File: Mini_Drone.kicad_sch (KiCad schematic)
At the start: 78 parts, among them J1 Conn_01x02, J3 Conn_01x02, J4 Conn_01x06, J7 Conn_01x11, J8 Conn_01x11, Q1 AO3400A, Q2 AO3400A, Q3 AO3400A, Q4 AO3400A, U1 ESP32-S3-WROOM-1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

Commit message: final checking and then order
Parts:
- removed R10, R12, R13, R14: 220, Resistor_SMD:R_0201_0603Metric, symbol Mini_Drone_prj:R
- added R12, R15, R16, R17: 220, Resistor_SMD:R_0603_1608Metric, symbol Device:R
- S2: footprint 500SSP1S1M2REA:SW_500SSP1S1M2REA -> Mini_Drone_prj:slide swithc
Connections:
- net BAT+: now also R12.1
- net GND: now also R15.1, R16.1, R17.1
- net at D5.1 (K): now also R17.2
- net at D1.1 (K): now also R16.2
- net at D7.1 (K): now also R15.2
- net at D8.2 (A): now also R12.2

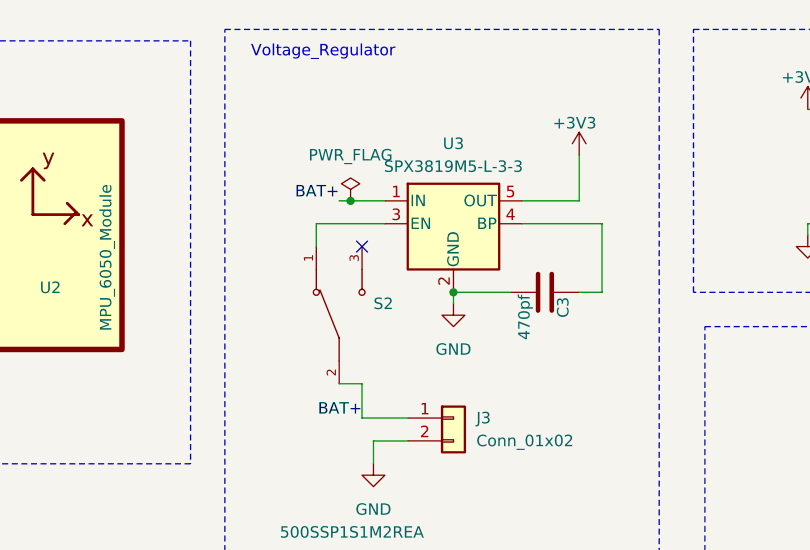
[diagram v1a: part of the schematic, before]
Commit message: added gnd to the switch other terminal
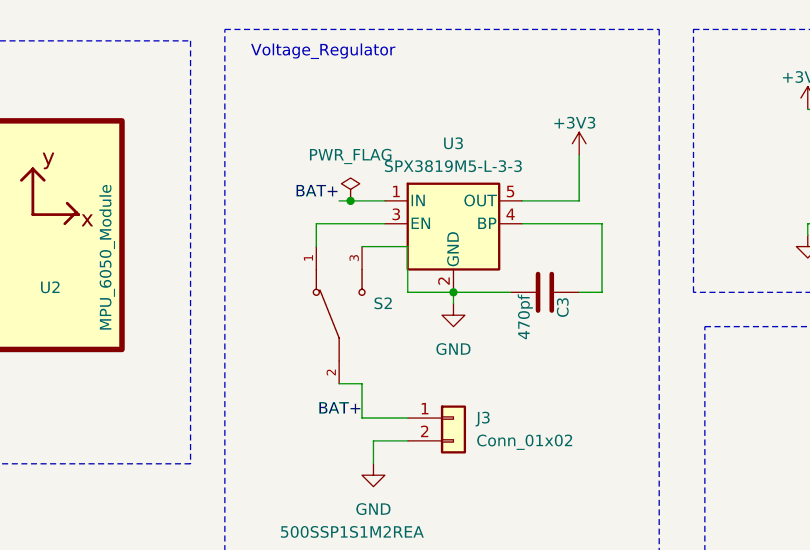
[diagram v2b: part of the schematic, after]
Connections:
- net GND: now also S2.3
- no-connect marks 5 -> 4
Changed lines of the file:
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@@
-	)
-	(no_connect
-		(at 207.01 43.18)
 	)
 	(no_connect
@@
 	(wire
 		(pts
+			(xy 212.09 48.26) (xy 217.17 48.26)
+		)
+		(stroke
+			(width 0)
+			(type default)
+		)
+	)
+	(wire
+		(pts
 			(xy 30.48 242.57) (xy 39.37 242.57)
 		)
@@
 	(wire
 		(pts
+			(xy 207.01 43.18) (xy 212.09 43.18)
+		)
+		(stroke
+			(width 0)
+			(type default)
+		)
+	)
+	(wire
+		(pts
 			(xy 243.84 236.22) (xy 243.84 232.41)
 		)
@@
 		)
 		(stroke
+			(width 0)
+			(type default)
+		)
+	)
+	(wire
+		(pts
+			(xy 212.09 43.18) (xy 212.09 48.26)
+		)
+		(stroke

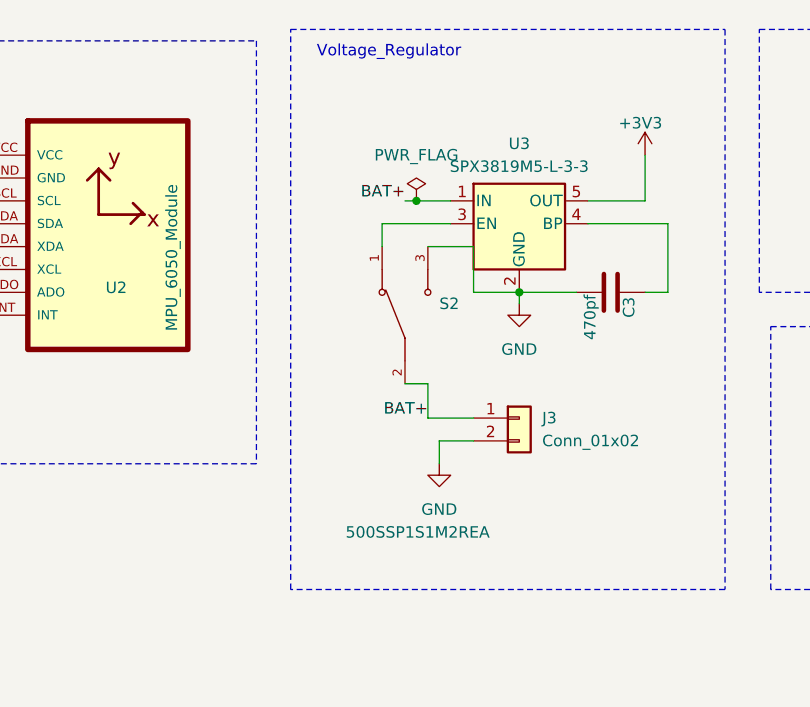
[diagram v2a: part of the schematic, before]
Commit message: switch connection has been corrected and the  polygon pour  has been reduced  to one layer for gnd and the connection is set to thermaal relief  for  easier soldering
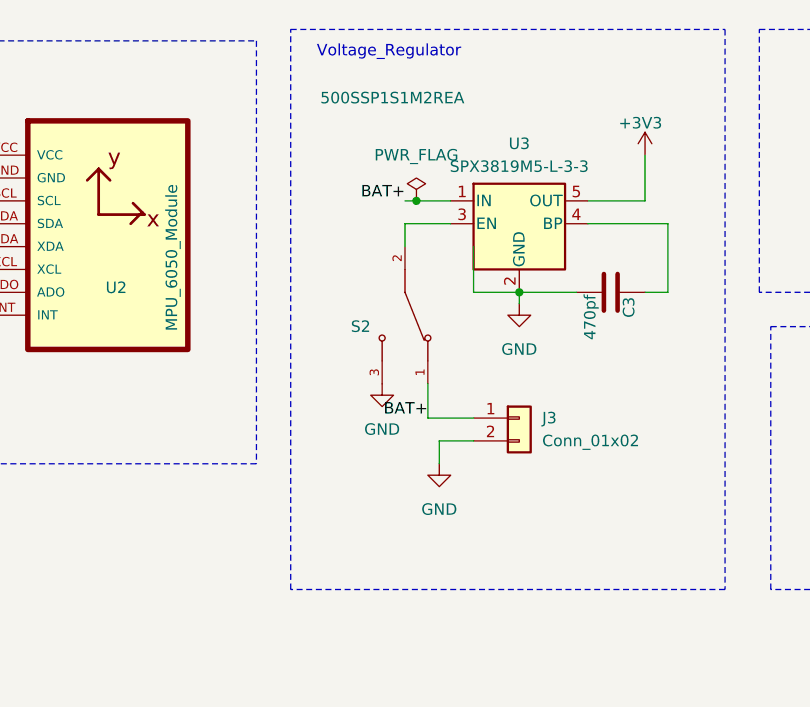
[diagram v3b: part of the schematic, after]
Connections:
- net BAT+: now also S2.1; no longer S2.2
- net at U3.3 (EN): now also S2.2; no longer S2.1
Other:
- moved on the sheet: S2
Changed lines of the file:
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@@
 	(wire
 		(pts
-			(xy 201.93 43.18) (xy 201.93 40.64)
-		)
-		(stroke
-			(width 0)
-			(type default)
-		)
-	)
-	(wire
-		(pts
 			(xy 39.37 242.57) (xy 48.26 242.57)
 		)
@@
 	(wire
 		(pts
-			(xy 207.01 43.18) (xy 212.09 43.18)
-		)
-		(stroke
-			(width 0)
-			(type default)
-		)
-	)
-	(wire
-		(pts
 			(xy 243.84 236.22) (xy 243.84 232.41)
 		)
@@
 	(wire
 		(pts
-			(xy 207.01 58.42) (xy 207.01 62.23)
+			(xy 160.02 227.33) (xy 166.37 227.33)
 		)
 		(stroke
@@
 	(wire
 		(pts
-			(xy 160.02 227.33) (xy 166.37 227.33)
+			(xy 31.75 90.17) (xy 31.75 87.63)
 		)
 		(stroke
@@
 	(wire
 		(pts
-			(xy 31.75 90.17) (xy 31.75 87.63)
+			(xy 148.59 132.08) (xy 148.59 137.16)
 		)
 		(stroke
@@
 	(wire
 		(pts
-			(xy 148.59 132.08) (xy 148.59 137.16)
+			(xy 204.47 43.18) (xy 204.47 40.64)
+		)
+		(stroke
+			(width 0)
+			(type default)
+		)
+	)
+	(wire
+		(pts
+			(xy 204.47 40.64) (xy 209.55 40.64)
 		)
 		(stroke
@@
 	(wire
 		(pts
-			(xy 31.75 33.02) (xy 41.91 33.02)
+			(xy 207.01 58.42) (xy 207.01 62.23)
 		)
 		(stroke
@@
 	(wire
 		(pts
-			(xy 34.29 54.61) (xy 29.21 54.61)
+			(xy 31.75 33.02) (xy 41.91 33.02)
 		)
 		(stroke
@@
 	(wire
 		(pts
-			(xy 233.68 40.64) (xy 233.68 48.26)
+			(xy 34.29 54.61) (xy 29.21 54.61)
 		)
 		(stroke
@@
 	(wire
 		(pts
-			(xy 95.25 162.56) (xy 107.95 162.56)
+			(xy 233.68 40.64) (xy 233.68 48.26)
 		)
 		(stroke
@@
 	(wire
 		(pts
-			(xy 247.65 232.41) (xy 254 232.41)
+			(xy 95.25 162.56) (xy 107.95 162.56)
 		)
 		(stroke
@@
 	(wire
 		(pts
-			(xy 49.53 90.17) (xy 52.07 90.17)
+			(xy 247.65 232.41) (xy 254 232.41)
 		)
 		(stroke
@@
 	(wire
 		(pts
-			(xy 204.47 58.42) (xy 207.01 58.42)
+			(xy 49.53 90.17) (xy 52.07 90.17)
 		)
 		(stroke
@@
 	(wire
 		(pts
-			(xy 201.93 40.64) (xy 209.55 40.64)
-		)
-		(stroke
-			(width 0)
-			(type default)
-		)
-	)
-	(wire
-		(pts
 			(xy 224.79 228.6) (xy 224.79 224.79)
 		)
@@
 	)
 	(symbol
+		(lib_id "power:GND")
+		(at 201.93 58.42 0)
+		(unit 1)
+		(exclude_from_sim no)
+		(in_bom yes)
+		(on_board yes)
+		(dnp no)
+		(fields_autoplaced yes)
+		(property "Reference" "#PWR024"
+			(at 201.93 64.77 0)
+			(effects
+				(font
+					(size 1.27 1.27)
+				)
+				(hide yes)
+			)
+		)
+		(property "Value" "GND"
+			(at 201.93 63.5 0)
+			(effects
+				(font
+					(size 1.27 1.27)
+				)
+			)
+		)
+		(property "Footprint" ""
+			(at 201.93 58.42 0)
+			(effects
+				(font
+					(size 1.27 1.27)
+				)
+				(hide yes)
+			)
+		)
+		(property "Datasheet" ""
+			(at 201.93 58.42 0)
+			(effects
+				(font
+					(size 1.27 1.27)
+				)
+				(hide yes)
+			)
+		)
+		(property "Description" "Power symbol creates a global label with name \"GND\" , ground"
+			(at 201.93 58.42 0)
+			(effects
+				(font
+					(size 1.27 1.27)
+				)
+				(hide yes)
+			)
+		)
+		(pin "1"
+		)
+		(instances
+			(project "Mini_Drone"
+				(path "/d47445ad-10e9-49aa-a867-c91f8f8ff1e7"
+					(reference "#PWR024")
+					(unit 1)
+				)
+			)
+		)
+	)
+	(symbol
 		(lib_id "Connector:TestPoint")
 		(at 48.26 138.43 180)
@@
 	(symbol
 		(lib_id "Mini_Drone_prj:500SSP1S1M2REA")
-		(at 204.47 50.8 90)
+		(at 204.47 50.8 270)
 		(unit 1)
 		(exclude_from_sim no)
@@
 		(dnp no)
 		(property "Reference" "S2"
-			(at 208.28 49.5299 90)
+			(at 200.66 52.0701 90)
 			(effects
 				(font
@@
 		)
 		(property "Value" "500SSP1S1M2REA"
-			(at 197.866 74.93 90)
+			(at 211.074 26.67 90)
 			(effects
 				(font

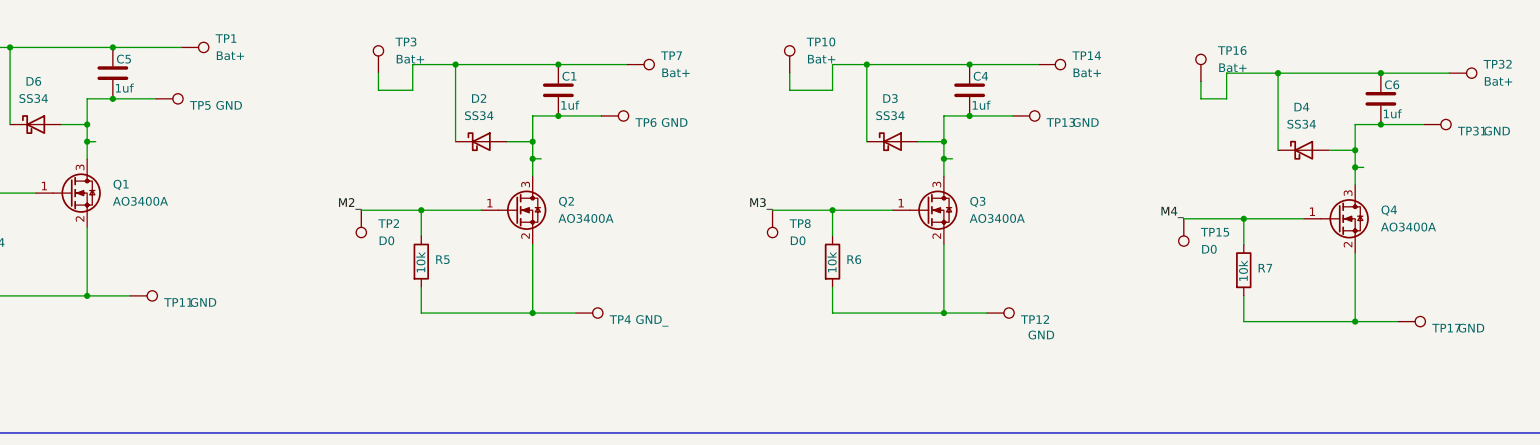
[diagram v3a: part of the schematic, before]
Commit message: smd pads has been changed to through hole pad and silkscreen has been arranged
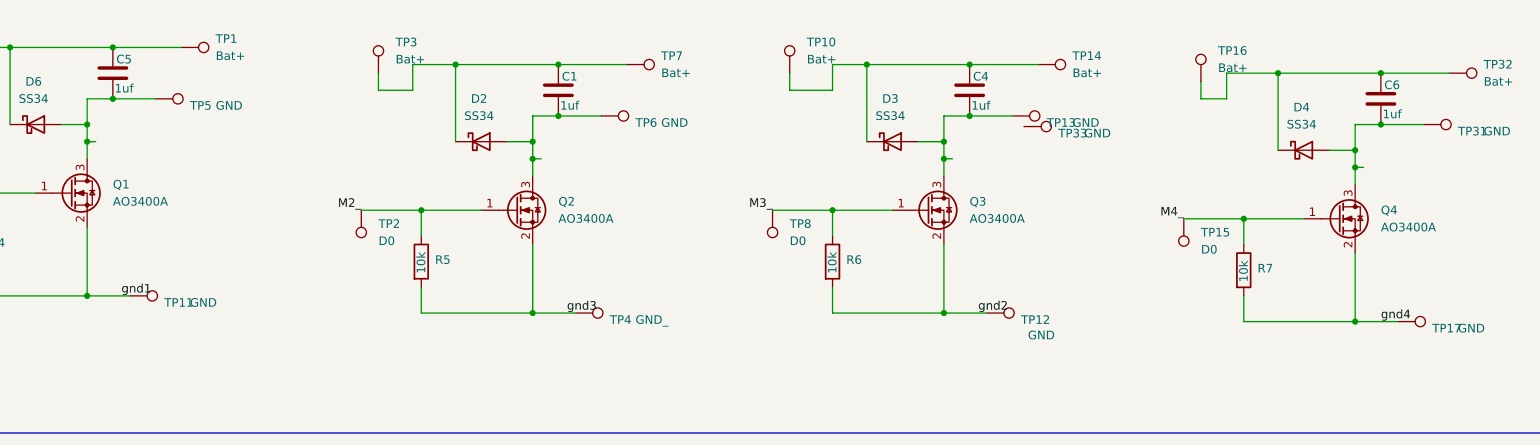
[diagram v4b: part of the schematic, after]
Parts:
- added TP33: GND, TestPoint:TestPoint_THTPad_2.0x2.0mm_Drill1.0mm, symbol Connector:TestPoint
- TP1, TP10, TP11, TP12, TP13, TP14, TP15, TP16, TP17, TP2, TP3, TP30, TP31, TP32, TP4, TP5, TP6, TP7, TP8, TP9: footprint TestPoint:TestPoint_Pad_D1.0mm -> TestPoint:TestPoint_THTPad_2.0x2.0mm_Drill1.0mm
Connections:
- net gnd1: now reaches Q1.2 (S), R4.2, TP11.1
- net gnd2: now reaches Q3.2 (S), R6.2, TP12.1
- net gnd4: now reaches Q4.2 (S), R7.2, TP17.1
- net gnd3: now reaches Q2.2 (S), R5.2, TP4.1
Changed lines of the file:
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@@
 		)
 	)
+	(label "gnd4"
+		(at 247.65 261.62 0)
+		(effects
+			(font
+				(size 1.27 1.27)
+			)
+			(justify left bottom)
+		)
+	)
 	(label "IO0"
 		(at 24.13 74.93 0)
@@
 		)
 	)
+	(label "gnd3"
+		(at 127 260.35 0)
+		(effects
+			(font
+				(size 1.27 1.27)
+			)
+			(justify left bottom)
+		)
+	)
 	(label "IO41"
 		(at 91.44 71.12 0)
@@
 		)
 	)
+	(label "gnd1"
+		(at 60.96 257.81 0)
+		(effects
+			(font
+				(size 1.27 1.27)
+			)
+			(justify left bottom)
+		)
+	)
 	(label "BAT+"
 		(at 207.01 62.23 180)
@@
 		)
 	)
+	(label "gnd2"
+		(at 187.96 260.35 0)
+		(effects
+			(font
+				(size 1.27 1.27)
+			)
+			(justify left bottom)
+		)
+	)
 	(label "EN"
 		(at 262.89 30.48 180)
@@
 			)
 		)
-		(property "Footprint" "TestPoint:TestPoint_Pad_D1.0mm"
+		(property "Footprint" "TestPoint:TestPoint_THTPad_2.0x2.0mm_Drill1.0mm"
 			(at 152.4 245.11 0)
 			(effects
@@
 			)
 		)
-		(property "Footprint" "TestPoint:TestPoint_Pad_D1.0mm"
+		(property "Footprint" "TestPoint:TestPoint_THTPad_2.0x2.0mm_Drill1.0mm"
 			(at 193.04 236.22 0)
 			(effects
@@
 			)
 		)
-		(property "Footprint" "TestPoint:TestPoint_Pad_D1.0mm"
+		(property "Footprint" "TestPoint:TestPoint_THTPad_2.0x2.0mm_Drill1.0mm"
 			(at 189.23 265.43 0)
 			(effects
@@
 			)
 		)
-		(property "Footprint" "TestPoint:TestPoint_Pad_D1.0mm"
+		(property "Footprint" "TestPoint:TestPoint_THTPad_2.0x2.0mm_Drill1.0mm"
 			(at 62.23 262.89 0)
 			(effects
@@
 			)
 		)
-		(property "Footprint" "TestPoint:TestPoint_Pad_D1.0mm"
+		(property "Footprint" "TestPoint:TestPoint_THTPad_2.0x2.0mm_Drill1.0mm"
 			(at 66.04 233.68 0)
 			(effects
@@
 			)
 		)
-		(property "Footprint" "TestPoint:TestPoint_Pad_D1.0mm"
+		(property "Footprint" "TestPoint:TestPoint_THTPad_2.0x2.0mm_Drill1.0mm"
 			(at 213.36 246.38 0)
 			(effects
@@
 	(symbol
 		(lib_id "Connector:TestPoint")
+		(at 194.7512 232.7095 270)
+		(unit 1)
+		(exclude_from_sim no)
+		(in_bom no)
+		(on_board yes)
+		(dnp no)
+		(property "Reference" "TP33"
+			(at 199.8312 233.7255 90)
+			(effects
+				(font
+					(size 1.27 1.27)
+				)
+				(justify left)
+			)
+		)
+		(property "Value" "GND"
+			(at 203.6412 233.7255 90)
+			(effects
+				(font
+					(size 1.27 1.27)
+				)
+				(justify left)
+			)
+		)
+		(property "Footprint" "TestPoint:TestPoint_THTPad_2.0x2.0mm_Drill1.0mm"
+			(at 194.7512 237.7895 0)
+			(effects
+				(font
+					(size 1.27 1.27)
+				)
+				(hide yes)
+			)
+		)
+		(property "Datasheet" "~"
+			(at 194.7512 237.7895 0)
+			(effects
+				(font
+					(size 1.27 1.27)
+				)
+				(hide yes)
+			)
+		)
+		(property "Description" "test point"
+			(at 194.7512 232.7095 0)
+			(effects
+				(font
+					(size 1.27 1.27)
+				)
+				(hide yes)
+			)
+		)
+		(pin "1"
+		)
+		(instances
+			(project "Mini_Drone"
+				(path "/d47445ad-10e9-49aa-a867-c91f8f8ff1e7"
+					(reference "TP33")
+					(unit 1)
+				)
+			)
+		)
+	)
+	(symbol
+		(lib_id "Connector:TestPoint")
 		(at 120.65 162.56 180)
 		(unit 1)
@@
 			)
 		)
-		(property "Footprint" "TestPoint:TestPoint_Pad_D1.0mm"
+		(property "Footprint" "TestPoint:TestPoint_THTPad_2.0x2.0mm_Drill1.0mm"
 			(at 135.89 228.6 0)
 			(effects
@@
 			)
 		)
-		(property "Footprint" "TestPoint:TestPoint_Pad_D1.0mm"
+		(property "Footprint" "TestPoint:TestPoint_THTPad_2.0x2.0mm_Drill1.0mm"
 			(at 250.19 266.7 0)
 			(effects
@@
 			)
 		)
-		(property "Footprint" "TestPoint:TestPoint_Pad_D1.0mm"
+		(property "Footprint" "TestPoint:TestPoint_THTPad_2.0x2.0mm_Drill1.0mm"
 			(at 69.85 226.06 0)
 			(effects
@@
 			)
 		)
-		(property "Footprint" "TestPoint:TestPoint_Pad_D1.0mm"
+		(property "Footprint" "TestPoint:TestPoint_THTPad_2.0x2.0mm_Drill1.0mm"
 			(at 25.4 242.57 0)
 			(effects
@@
 			)
 		)
-		(property "Footprint" "TestPoint:TestPoint_Pad_D1.0mm"
+		(property "Footprint" "TestPoint:TestPoint_THTPad_2.0x2.0mm_Drill1.0mm"
 			(at 257.81 229.87 0)
 			(effects
@@
 			)
 		)
-		(property "Footprint" "TestPoint:TestPoint_Pad_D1.0mm"
+		(property "Footprint" "TestPoint:TestPoint_THTPad_2.0x2.0mm_Drill1.0mm"
 			(at 91.44 245.11 0)
 			(effects
@@
 			)
 		)
-		(property "Footprint" "TestPoint:TestPoint_Pad_D1.0mm"
+		(property "Footprint" "TestPoint:TestPoint_THTPad_2.0x2.0mm_Drill1.0mm"
 			(at 165.1 224.79 0)
 			(effects
@@
 			)
 		)
-		(property "Footprint" "TestPoint:TestPoint_Pad_D1.0mm"
+		(property "Footprint" "TestPoint:TestPoint_THTPad_2.0x2.0mm_Drill1.0mm"
 			(at 38.1 222.25 0)
 			(effects
@@
 			)
 		)
-		(property "Footprint" "TestPoint:TestPoint_Pad_D1.0mm"
+		(property "Footprint" "TestPoint:TestPoint_THTPad_2.0x2.0mm_Drill1.0mm"
 			(at 254 237.49 0)
 			(effects
@@
 			)
 		)
-		(property "Footprint" "TestPoint:TestPoint_Pad_D1.0mm"
+		(property "Footprint" "TestPoint:TestPoint_THTPad_2.0x2.0mm_Drill1.0mm"
 			(at 196.85 228.6 0)
 			(effects
@@
 			)
 		)
-		(property "Footprint" "TestPoint:TestPoint_Pad_D1.0mm"
+		(property "Footprint" "TestPoint:TestPoint_THTPad_2.0x2.0mm_Drill1.0mm"
 			(at 132.08 236.22 0)
 			(effects
@@
 			)
 		)
-		(property "Footprint" "TestPoint:TestPoint_Pad_D1.0mm"
+		(property "Footprint" "TestPoint:TestPoint_THTPad_2.0x2.0mm_Drill1.0mm"
 			(at 104.14 224.79 0)
 			(effects
@@
 			)
 		)
-		(property "Footprint" "TestPoint:TestPoint_Pad_D1.0mm"
+		(property "Footprint" "TestPoint:TestPoint_THTPad_2.0x2.0mm_Drill1.0mm"
 			(at 226.06 226.06 0)
 			(effects
@@
 			)
 		)
-		(property "Footprint" "TestPoint:TestPoint_Pad_D1.0mm"
+		(property "Footprint" "TestPoint:TestPoint_THTPad_2.0x2.0mm_Drill1.0mm"
 			(at 128.27 265.43 0)
 			(effects
